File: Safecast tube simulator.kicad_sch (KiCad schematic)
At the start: 11 parts, among them Q1 IXTH10P60, SW1 SW_Push, SW2 RotaryEncoder_Switch, U1 EL817, U2 SSD1306, U3 ESP32-WROOM-32U

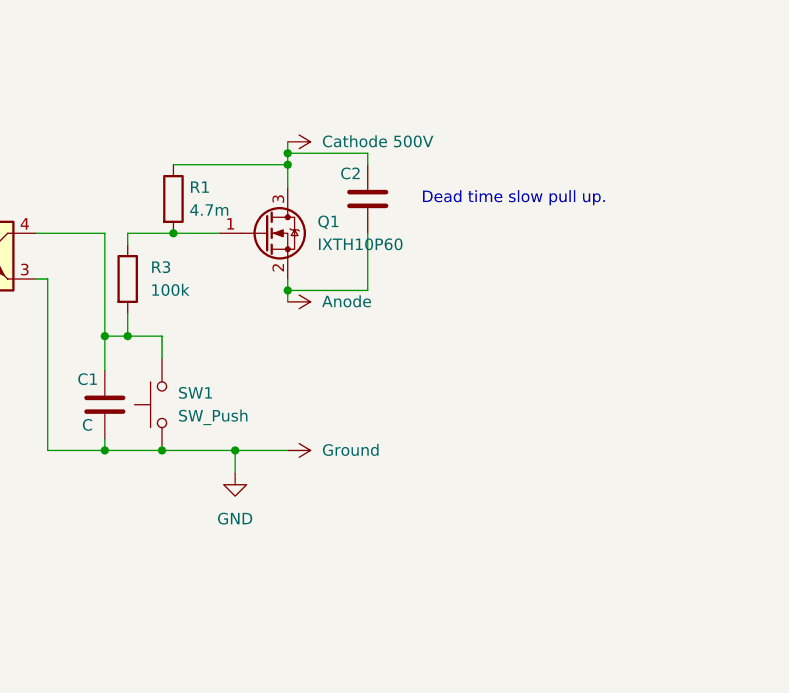
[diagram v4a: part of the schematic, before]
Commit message: Updated schematic with Toy his suggestions.
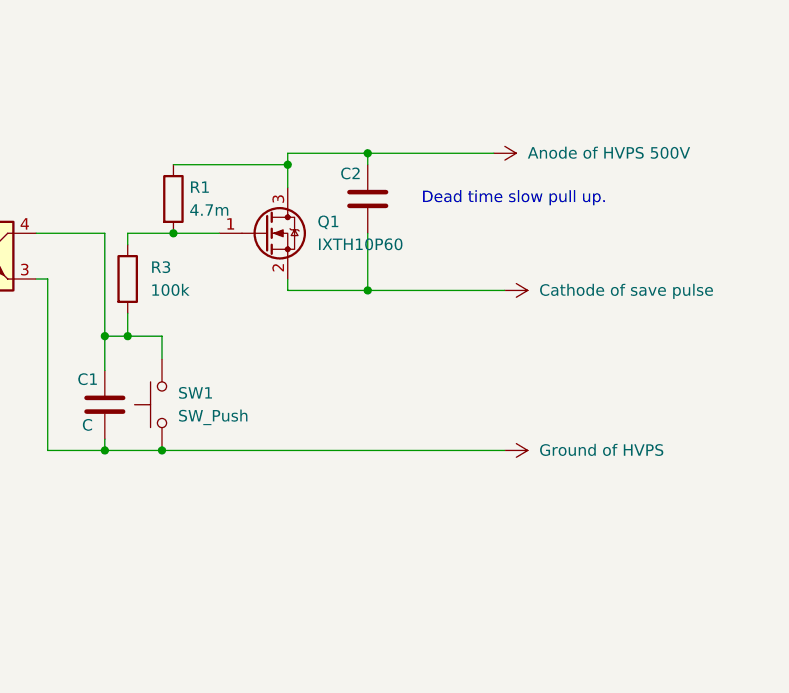
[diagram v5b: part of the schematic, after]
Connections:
- net GND: no longer C1.2, SW1.1, U1.3
- net Anode renamed Cathode of save pulse
- net Cathode 500V renamed Anode of HVPS 500V
- new net Ground of HVPS: C1.2, SW1.1, U1.3
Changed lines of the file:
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@@
 (kicad_sch (version 20230819) (generator eeschema)
   (paper "A4")
-  (junction (at 213.36 76.2) (diameter 0) (color 0 0 0 0)
-  )
   (junction (at 200.66 85.09) (diameter 0) (color 0 0 0 0)
   )
@@
   (junction (at 195.58 96.52) (diameter 0) (color 0 0 0 0)
   )
-  (junction (at 213.36 91.44) (diameter 0) (color 0 0 0 0)
+  (junction (at 222.25 91.44) (diameter 0) (color 0 0 0 0)
   )
   (junction (at 213.36 77.47) (diameter 0) (color 0 0 0 0)
   )
-  (junction (at 207.518 109.22) (diameter 0) (color 0 0 0 0)
+  (junction (at 222.25 76.2) (diameter 0) (color 0 0 0 0)
   )
   (junction (at 193.04 96.52) (diameter 0) (color 0 0 0 0)
@@
     (stroke (width 0) (type default))
   )
-  (wire (pts (xy 213.36 91.44) (xy 213.36 92.71))
-    (stroke (width 0) (type default))
-  )
   (wire (pts (xy 132.08 90.17) (xy 132.08 110.49))
     (stroke (width 0) (type default))
@@
     (stroke (width 0) (type default))
   )
-  (wire (pts (xy 207.518 109.22) (xy 213.36 109.22))
-    (stroke (width 0) (type default))
-  )
   (wire (pts (xy 195.58 85.09) (xy 195.58 86.36))
     (stroke (width 0) (type default))
@@
     (stroke (width 0) (type default))
   )
-  (wire (pts (xy 207.518 109.22) (xy 207.518 111.76))
-    (stroke (width 0) (type default))
-  )
   (wire (pts (xy 115.57 120.65) (xy 121.92 120.65))
     (stroke (width 0) (type default))
@@
     (stroke (width 0) (type default))
   )
+  (wire (pts (xy 236.22 76.2) (xy 222.25 76.2))
+    (stroke (width 0) (type default))
+  )
   (wire (pts (xy 115.57 110.49) (xy 132.08 110.49))
     (stroke (width 0) (type default))
@@
     (stroke (width 0) (type default))
   )
-  (wire (pts (xy 213.36 74.93) (xy 213.36 76.2))
-    (stroke (width 0) (type default))
-  )
   (wire (pts (xy 193.04 96.52) (xy 195.58 96.52))
     (stroke (width 0) (type default))
@@
     (stroke (width 0) (type default))
   )
-  (wire (pts (xy 199.39 109.22) (xy 207.518 109.22))
+  (wire (pts (xy 199.39 109.22) (xy 237.49 109.22))
     (stroke (width 0) (type default))
   )
@@
   )
   (wire (pts (xy 115.57 102.87) (xy 129.54 102.87))
+    (stroke (width 0) (type default))
+  )
+  (wire (pts (xy 237.49 91.44) (xy 222.25 91.44))
     (stroke (width 0) (type default))
   )
@@
     )
   )
-  (symbol (lib_id "power:+5V") (at 213.36 74.93 270) (unit 1)
-    (exclude_from_sim no) (in_bom yes) (on_board yes) (dnp no) (fields_autoplaced)
-    (property "Reference" "#PWR01" (at 209.55 74.93 0)
-      (effects (font (size 1.27 1.27)) hide)
-    )
-    (property "Value" "Cathode 500V" (at 217.17 74.9299 90)
-      (effects (font (size 1.27 1.27)) (justify left))
-    )
-    (property "Footprint" "" (at 213.36 74.93 0)
-      (effects (font (size 1.27 1.27)) hide)
-    )
-    (property "Datasheet" "" (at 213.36 74.93 0)
-      (effects (font (size 1.27 1.27)) hide)
-    )
-    (property "Description" "Power symbol creates a global label with name \"+5V\"" (at 213.36 74.93 0)
+  (symbol (lib_id "power:+5V") (at 236.22 76.2 270) (unit 1)
+    (exclude_from_sim no) (in_bom yes) (on_board yes) (dnp no) (fields_autoplaced)
+    (property "Reference" "#PWR01" (at 232.41 76.2 0)
+      (effects (font (size 1.27 1.27)) hide)
+    )
+    (property "Value" "Anode of HVPS 500V" (at 240.03 76.1999 90)
+      (effects (font (size 1.27 1.27)) (justify left))
+    )
+    (property "Footprint" "" (at 236.22 76.2 0)
+      (effects (font (size 1.27 1.27)) hide)
+    )
+    (property "Datasheet" "" (at 236.22 76.2 0)
+      (effects (font (size 1.27 1.27)) hide)
+    )
+    (property "Description" "Power symbol creates a global label with name \"+5V\"" (at 236.22 76.2 0)
       (effects (font (size 1.27 1.27)) hide)
     )
@@
     )
   )
-  (symbol (lib_id "power:+5V") (at 213.36 92.71 270) (unit 1)
-    (exclude_from_sim no) (in_bom yes) (on_board yes) (dnp no) (fields_autoplaced)
-    (property "Reference" "#PWR02" (at 209.55 92.71 0)
-      (effects (font (size 1.27 1.27)) hide)
-    )
-    (property "Value" "Anode" (at 217.17 92.7099 90)
-      (effects (font (size 1.27 1.27)) (justify left))
-    )
-    (property "Footprint" "" (at 213.36 92.71 0)
-      (effects (font (size 1.27 1.27)) hide)
-    )
-    (property "Datasheet" "" (at 213.36 92.71 0)
-      (effects (font (size 1.27 1.27)) hide)
-    )
-    (property "Description" "Power symbol creates a global label with name \"+5V\"" (at 213.36 92.71 0)
+  (symbol (lib_id "power:+5V") (at 237.49 91.44 270) (unit 1)
+    (exclude_from_sim no) (in_bom yes) (on_board yes) (dnp no) (fields_autoplaced)
+    (property "Reference" "#PWR02" (at 233.68 91.44 0)
+      (effects (font (size 1.27 1.27)) hide)
+    )
+    (property "Value" "Cathode of save pulse" (at 241.3 91.4399 90)
+      (effects (font (size 1.27 1.27)) (justify left))
+    )
+    (property "Footprint" "" (at 237.49 91.44 0)
+      (effects (font (size 1.27 1.27)) hide)
+    )
+    (property "Datasheet" "" (at 237.49 91.44 0)
+      (effects (font (size 1.27 1.27)) hide)
+    )
+    (property "Description" "Power symbol creates a global label with name \"+5V\"" (at 237.49 91.44 0)
       (effects (font (size 1.27 1.27)) hide)
     )
@@
         (path "/757f8051-c0f1-48f3-a28e-7f57f8c03b8d"
           (reference "#PWR07") (unit 1)
-        )
-      )
-    )
-  )
-  (symbol (lib_id "power:GND") (at 207.518 111.76 0) (unit 1)
-    (exclude_from_sim no) (in_bom yes) (on_board yes) (dnp no) (fields_autoplaced)
-    (property "Reference" "#PWR04" (at 207.518 118.11 0)
-      (effects (font (size 1.27 1.27)) hide)
-    )
-    (property "Value" "GND" (at 207.518 116.84 0)
-      (effects (font (size 1.27 1.27)))
-    )
-    (property "Footprint" "" (at 207.518 111.76 0)
-      (effects (font (size 1.27 1.27)) hide)
-    )
-    (property "Datasheet" "" (at 207.518 111.76 0)
-      (effects (font (size 1.27 1.27)) hide)
-    )
-    (property "Description" "Power symbol creates a global label with name \"GND\" , ground" (at 207.518 111.76 0)
-      (effects (font (size 1.27 1.27)) hide)
-    )
-    (pin "1")
-    (instances
-      (project "Safecast tube simulator"
-        (path "/757f8051-c0f1-48f3-a28e-7f57f8c03b8d"
-          (reference "#PWR04") (unit 1)
         )
       )
@@
     )
   )
-  (symbol (lib_id "power:+5V") (at 213.36 109.22 270) (unit 1)
-    (exclude_from_sim no) (in_bom yes) (on_board yes) (dnp no) (fields_autoplaced)
-    (property "Reference" "#PWR05" (at 209.55 109.22 0)
-      (effects (font (size 1.27 1.27)) hide)
-    )
-    (property "Value" "Ground" (at 217.17 109.2199 90)
-      (effects (font (size 1.27 1.27)) (justify left))
-    )
-    (property "Footprint" "" (at 213.36 109.22 0)
-      (effects (font (size 1.27 1.27)) hide)
-    )
-    (property "Datasheet" "" (at 213.36 109.22 0)
-      (effects (font (size 1.27 1.27)) hide)
-    )
-    (property "Description" "Power symbol creates a global label with name \"+5V\"" (at 213.36 109.22 0)
-      (effects (font (size 1.27 1.27)) hide)
-    )
+  (symbol (lib_id "power:+5V") (at 237.49 109.22 270) (unit 1)
+    (exclude_from_sim no) (in_bom yes) (on_board yes) (dnp no) (fields_autoplaced)
+    (property "Reference" "#PWR05" (at 233.68 109.22 0)
+      (effects (font (size 1.27 1.27)) hide)
+    )
+    (property "Value" "Ground of HVPS" (at 241.3 109.2199 90)
+      (effects (font (size 1.27 1.27)) (justify left))
+    )
+    (property "Footprint" "" (at 237.49 109.22 0)
+      (effects (font (size 1.27 1.27)) hide)
+    )
+    (property "Datasheet" "" (at 237.49 109.22 0)
+      (effects (font (size 1.27 1.27)) hide)
+    )
+    (property "Description" "Power symbol creates a global label with name \"+5V\"" (at 237.49 109.22 0)
+      (effects (font (size 1.27 1.27)) hide)
+    )
